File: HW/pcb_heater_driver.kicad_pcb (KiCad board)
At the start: 2 copper layers, 160 x 100 mm, 68 parts, among them J1 Heater, J2 JTAG, J4 USB_C_Receptacle_USB2.0, J5 OLED, Q1 RQ3E110AJ, Q2 BC817, Q3 BC817, SW1 SW_SPST, SW2 SW_DPST, SW3 SW_DPST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

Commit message: revision 0
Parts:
- C2: value 200uF -> 200u
- C4: value 22nF -> 22n
- R1: value BR_DNP -> DNP
- R17: value TBD -> 0
- moved J4 0.34 mm to (77.1, 90.4)
- moved R19 0.10 mm to (99.3, 90.7)
- moved R20 0.10 mm to (104.3, 90.5)
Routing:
- net mosfet_gate: track 53.2 -> 51.0 mm
- net Net-(C4-Pad2): track 5.00 -> 2.88 mm
- net GND: track 119.9 -> 119.1 mm
- net /Peripherals/UART_USB_D-: track 14.3 -> 15.0 mm
- net /Heater/heater_LOW: track 52.8 -> 52.1 mm

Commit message: Readme and board fixes
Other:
- board text added: "+"
- board text added: "-"
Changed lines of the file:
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@@
     (property "Sheetname" "Heater")
     (attr through_hole)
-    (fp_text reference "Q1" (at 0 -3.116337 90) (layer "F.SilkS")
+    (fp_text reference "Q1" (at 3.134997 -0.029998 180) (layer "F.SilkS")
       (effects (font (size 1.001236 1.001236) (thickness 0.15)))
     )
@@
     (effects (font (size 1 1) (thickness 0.15)))
   )
+  (gr_text "-" (at 83.695987 65.782676 180) (layer "F.SilkS")
+    (effects (font (size 2 2) (thickness 0.3)))
+  )
   (gr_text "Data\nonly" (at 76.345987 97.632676) (layer "F.SilkS")
     (effects (font (size 1.2 1.2) (thickness 0.15)))
@@
     (effects (font (size 2 2) (thickness 0.3)))
   )
+  (gr_text "+" (at 83.695987 60.782676 90) (layer "F.SilkS")
+    (effects (font (size 2 2) (thickness 0.3)))
+  )

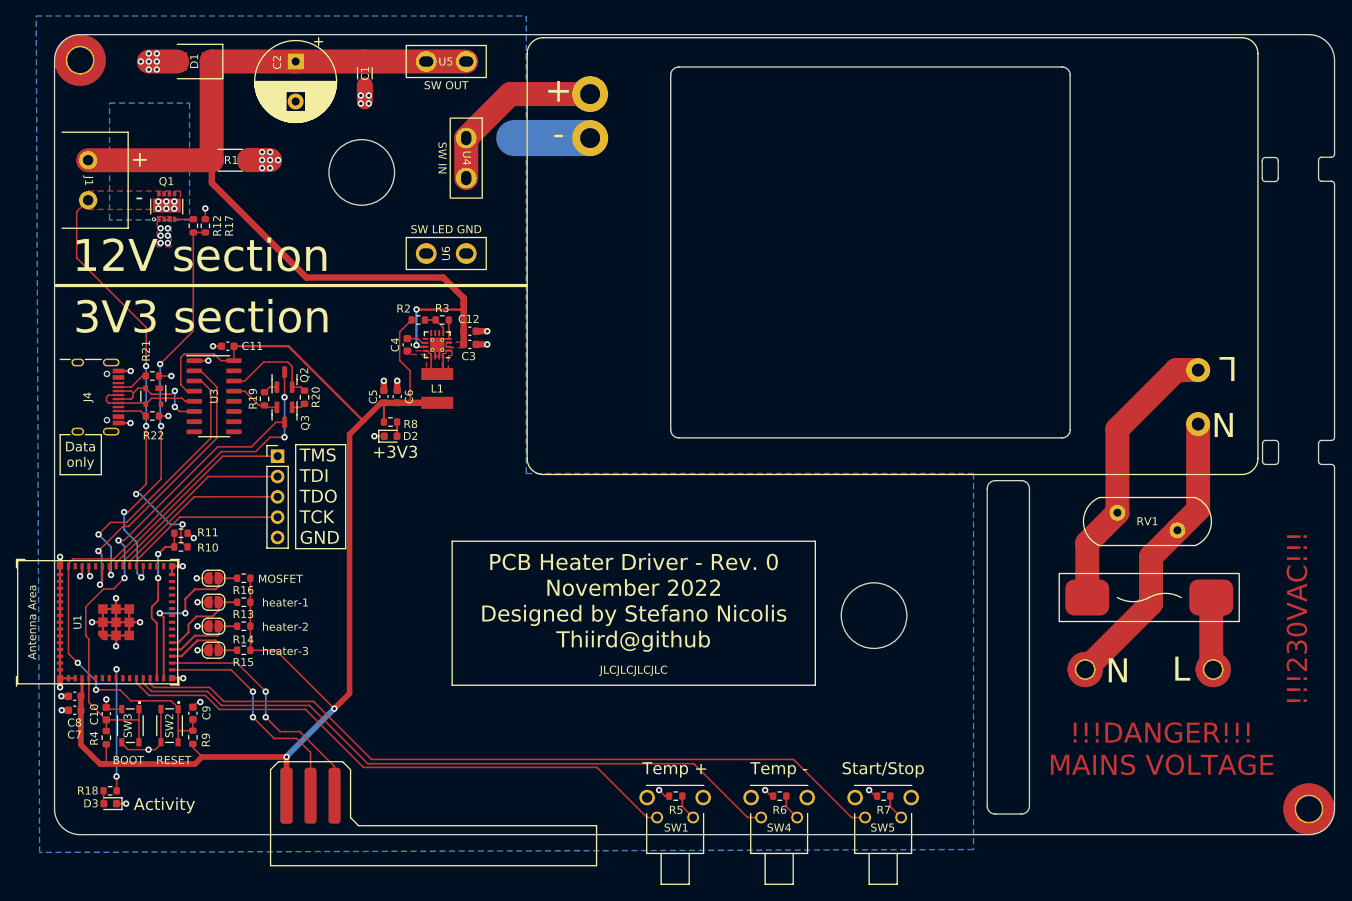
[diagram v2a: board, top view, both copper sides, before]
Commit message: Fixed silkscreen, removed one thermistor, fixed component placement
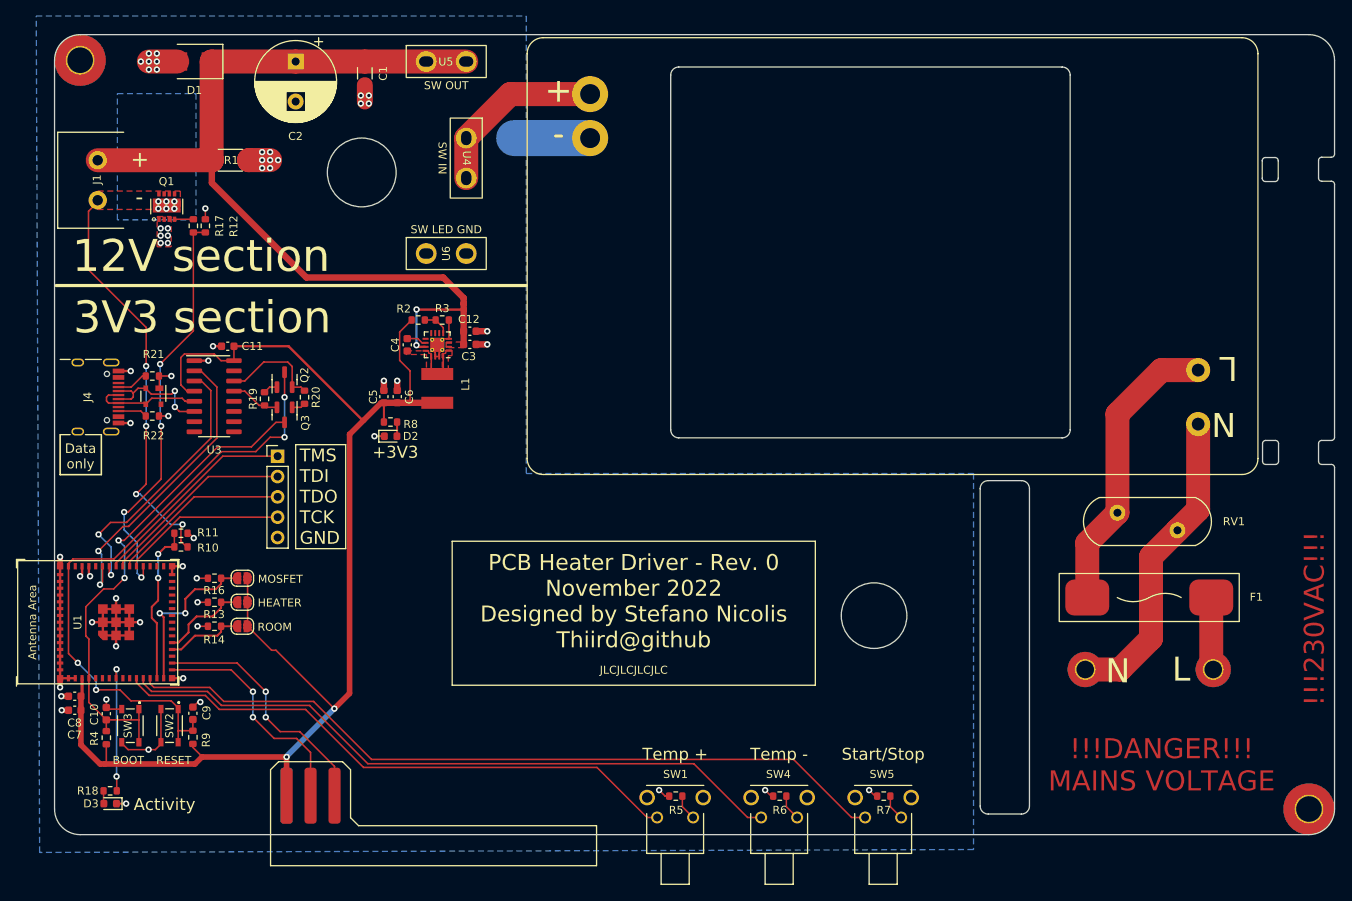
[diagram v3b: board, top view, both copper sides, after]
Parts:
- removed R15: 10k, Resistor_SMD:R_0603_1608Metric
- removed TH3: Heater_3, Jumper:SolderJumper-2_P1.3mm_Open_RoundedPad1.0x1.5mm
- C3: value 10uF -> 10u
- R3: value 37k -> 3k7
- TH1: value Heater_1 -> heater_temp
- TH2: value Heater_2 -> room_temp
- moved R13 3.66 mm to (93.1, 116.1)
- moved R14 3.66 mm to (93.1, 119.1)
- moved R16 3.66 mm to (93.1, 113.1)
- moved TH1 3.60 mm to (96.6, 116.1)
- moved TH2 3.60 mm to (96.6, 119.1)
- moved TH4 3.60 mm to (96.6, 113.1)
- moved J1 1.20 mm to (78.5, 63.3), turned to 90 degrees
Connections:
- J1 pad 1: +12V -> /Heater/heater_LOW
- J1 pad 2: /Heater/heater_LOW -> +12V
- R13 pad 1: +3V3 -> temp_heater_1
- R13 pad 2: temp_heater_1 -> GND
- R14 pad 1: +3V3 -> temp_heater_2
- R14 pad 2: temp_heater_2 -> GND
- R16 pad 1: +3V3 -> temp_mosfet
- R16 pad 2: temp_mosfet -> GND
- TH1 pad 1: GND -> temp_heater_1
- TH1 pad 2: temp_heater_1 -> +3V3
- TH2 pad 1: GND -> temp_heater_2
- TH2 pad 2: temp_heater_2 -> +3V3
- TH4 pad 1: GND -> temp_mosfet
- TH4 pad 2: temp_mosfet -> +3V3
- U1 pad 20: temp_heater_1 -> unconnected-(U1-Pad20)
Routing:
- net temp_heater_3: track 9.96 -> 0.00 mm
- net Net-(H7-Pad1): track 36.5 -> 39.1 mm
- net +3V3: track 171.6 -> 170.2 mm
- net GND: track 119.1 -> 117.8 mm, vias 60 -> 59
- net +12V: track 117.4 -> 116.2 mm
- net Net-(F1-Pad2): track 35.8 -> 36.9 mm
- net /Heater/heater_LOW: track 52.1 -> 51.5 mm
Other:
- outline, holes or cut-outs redrawn
- board text added: "HEATER"
- board text added: "ROOM"
- board text removed: "heater-1"
- board text removed: "heater-2"
- board text removed: "heater-3"

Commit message: Fixed component placement, enlarged some pcb slots, removed two thermistors
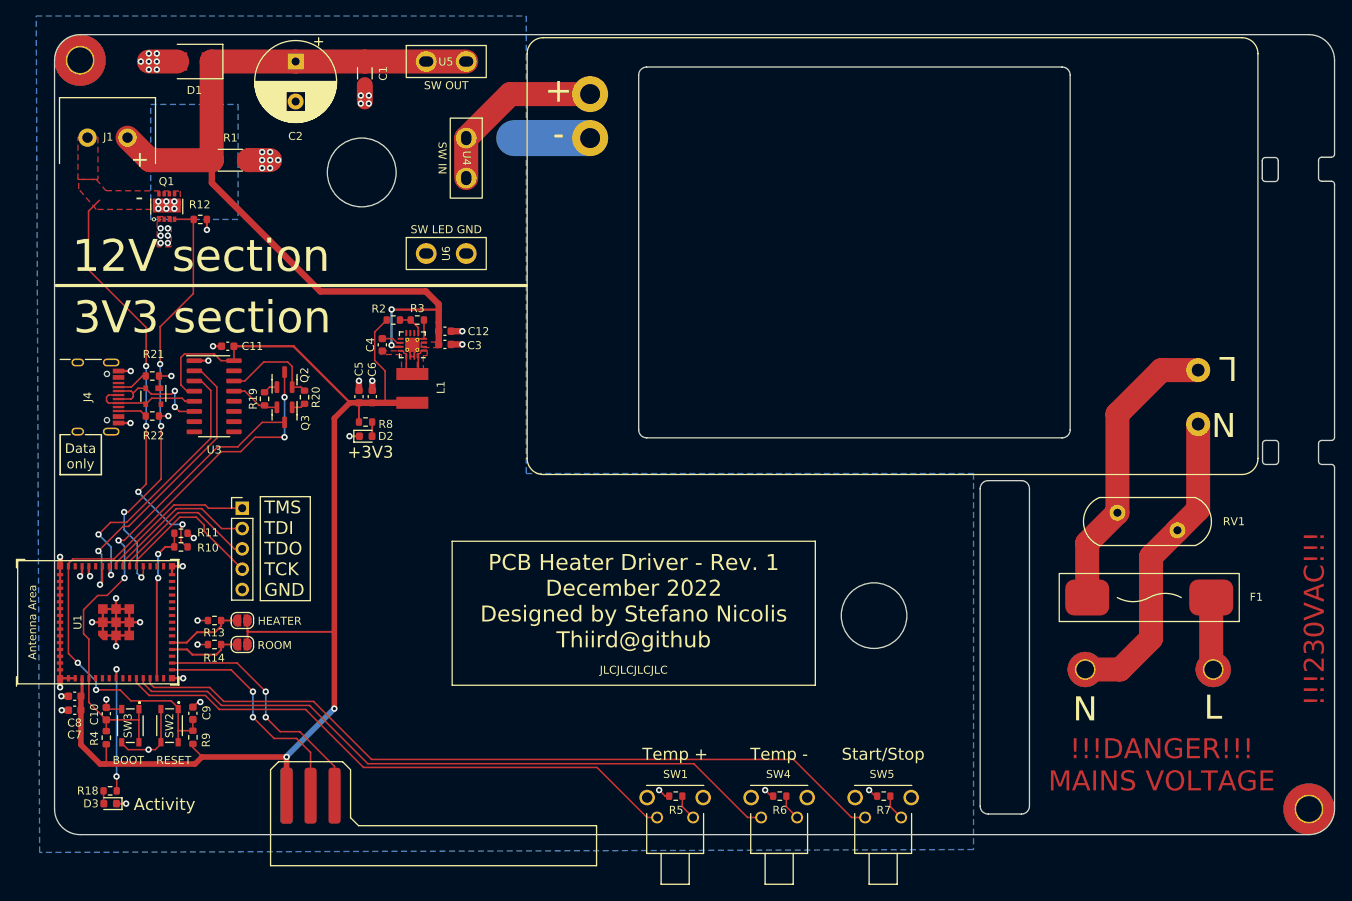
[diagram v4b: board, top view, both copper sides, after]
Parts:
- removed R16: 10k, Resistor_SMD:R_0603_1608Metric
- removed R17: 0, Resistor_SMD:R_0603_1608Metric
- removed TH4: mosfet, Jumper:SolderJumper-2_P1.3mm_Open_RoundedPad1.0x1.5mm
- moved J2 7.86 mm to (96.6, 104.3)
- moved J1 5.46 mm to (79.7, 58.0), turned to 0 degrees
- moved C12 3.12 mm to (121.9, 82.2)
- moved C3 3.12 mm to (121.9, 83.9)
- moved C4 3.12 mm to (114.1, 83.9)
- moved C5 3.12 mm to (111.2, 90.4)
- moved C6 3.12 mm to (112.8, 90.4)
- moved L1 3.12 mm to (117.8, 88.9)
- moved R2 3.12 mm to (115.4, 80.8)
- moved R3 3.12 mm to (118.4, 80.8)
- moved R8 3.12 mm to (112.0, 93.6)
- moved U2 3.12 mm to (117.8, 83.9)
- moved D2 3.12 mm to (112.0, 95.3)
- moved R13 2.28 mm to (93.1, 118.4)
- moved R14 2.28 mm to (93.1, 121.4)
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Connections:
- net temp_heater_2 renamed temp_room
- Q1 pad 2: Net-(Q1-Pad2) -> mosfet_gate
- R13 pad 1: temp_heater_1 -> temp_heater
- TH1 pad 1: temp_heater_1 -> temp_heater
- U1 pad 15: temp_mosfet -> unconnected-(U1-Pad15)
- U1 pad 18: temp_heater_3 -> unconnected-(U1-Pad18)
- U1 pad 20: unconnected-(U1-Pad20) -> temp_heater
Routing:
- net temp_mosfet: track 21.3 -> 0.00 mm, vias 2 -> 0
- net temp_heater_1: track 11.2 -> 0.00 mm
- net +3V3: track 170.2 -> 159.7 mm
- net temp_heater: track 0.00 -> 9.70 mm
- net /MCU/TMS: track 26.4 -> 19.6 mm
- net +12V: track 116.2 -> 110.0 mm
- net /MCU/TDI: track 24.3 -> 19.2 mm
- net /MCU/TDO: track 22.4 -> 19.1 mm
- net mosfet_gate: track 51.0 -> 53.5 mm
- net Net-(Q1-Pad2): track 2.35 -> 0.00 mm
- net GND: track 117.8 -> 116.3 mm, vias 59 -> 58
- net /MCU/TCK: track 20.6 -> 19.3 mm
- net current_sense_LOW: track 20.2 -> 19.7 mm
- net /Heater/heater_LOW: track 51.5 -> 51.0 mm
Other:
- outline, holes or cut-outs redrawn
- board text added: "PCB Heater Driver - Rev. 1 December 2022 Designed by Stefano Nicolis Thiird@github"
- board text removed: "MOSFET"
- board text removed: "PCB Heater Driver - Rev. 0 November 2022 Designed by Stefano Nicolis Thiird@github"
